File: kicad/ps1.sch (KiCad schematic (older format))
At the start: 35 parts

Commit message: Annotated, regenerated plot
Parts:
- gave numbers to parts that had none: 35
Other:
- moved on the sheet: C1, C10, C11, C12, C13, C14, C2, C3, C4, C5, C6, C7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

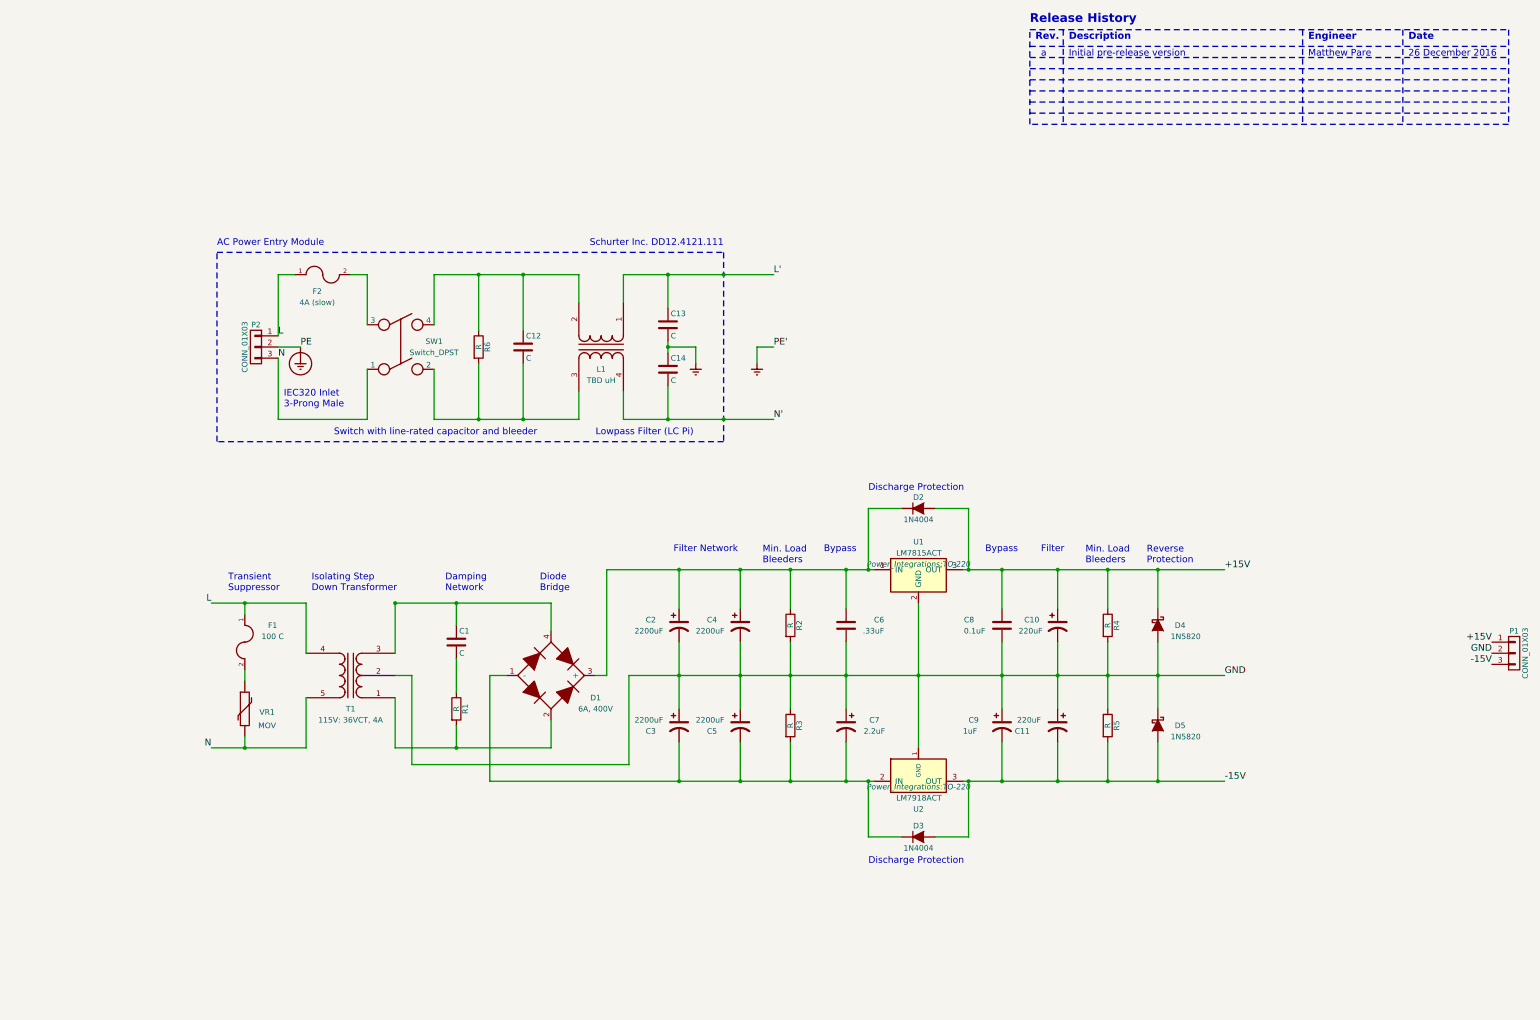
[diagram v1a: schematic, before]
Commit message: Removed power entry block as preparing for pcb layout.
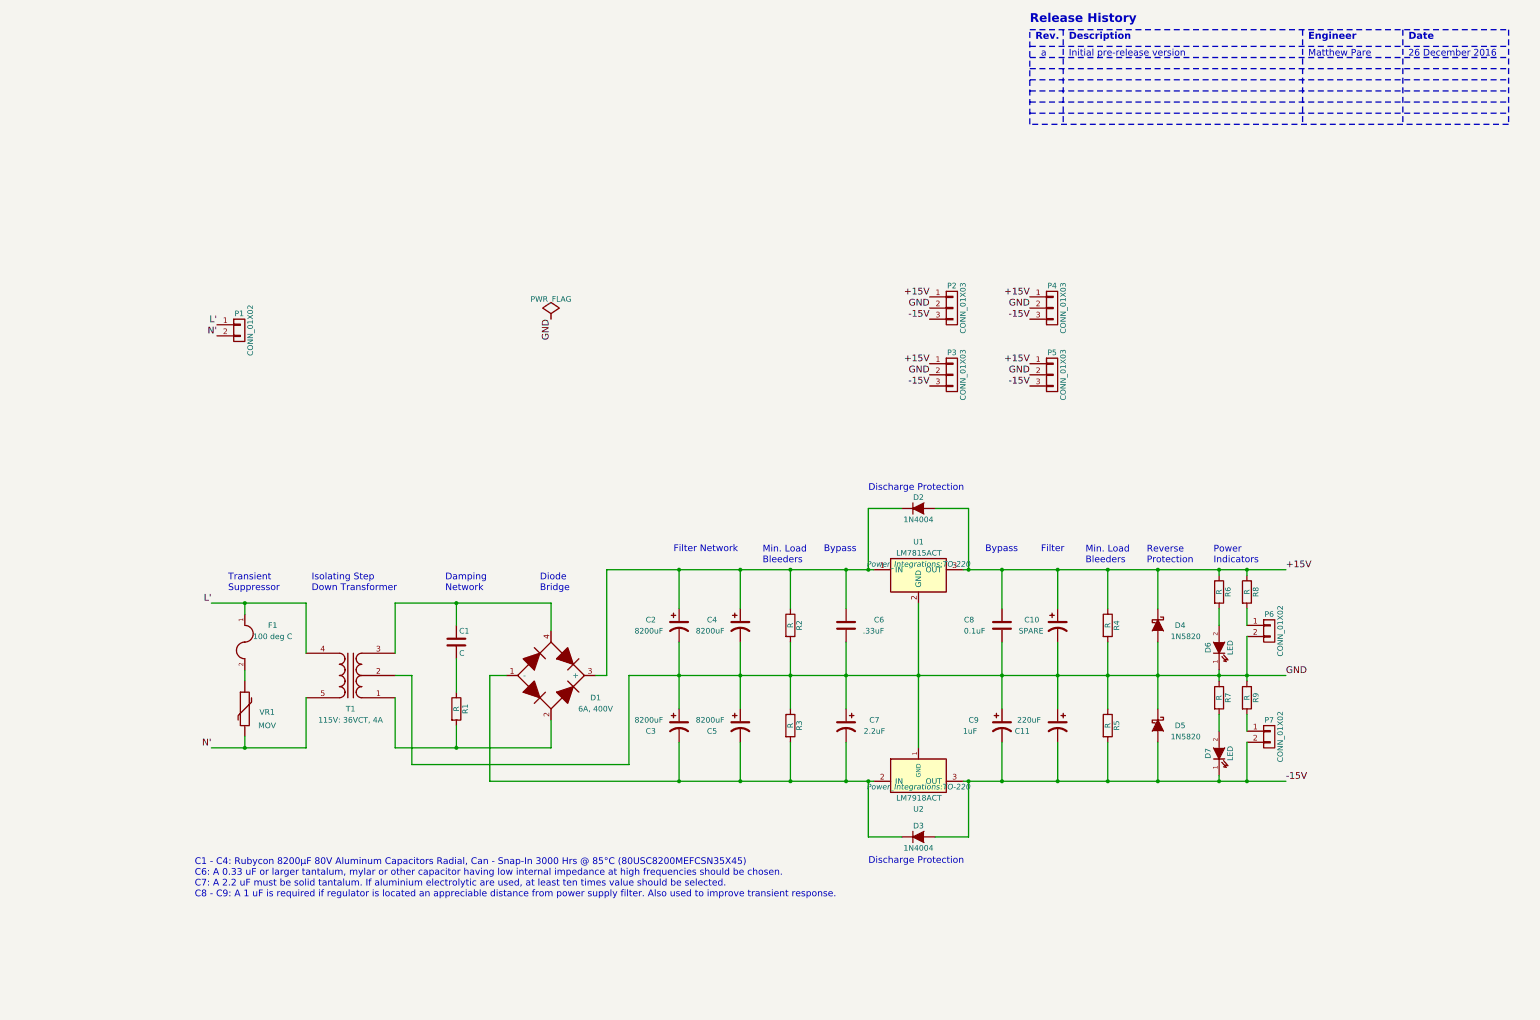
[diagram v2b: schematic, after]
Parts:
- removed C12, C13, C14: C, symbol C
- removed F2: 4A (slow), symbol FUSE
- removed L1: TBD uH, symbol TRANSFO
- removed P1: CONN_01X03, symbol CONN_01X03
- removed SW1: Switch_DPST, symbol Switch_DPST
- added D6, D7: LED, symbol LED
- added P1, P6, P7: CONN_01X02, symbol CONN_01X02
- added P3, P4, P5: CONN_01X03, symbol CONN_01X03
- added R7, R8, R9: R, symbol R
- C10: value 220uF -> SPARE
- C2, C3, C4, C5: value 2200uF -> 8200uF
- F1: value 100 C -> 100 deg C
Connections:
- net Earth_Protective is gone; now on net GND: P2.2 (P2)
- net +15V: now also P2.1 (P1), R6.1, P3.1 (P1), P4.1 (P1), P5.1 (P1), R8.1
- net -15V: now also P2.3 (P3), D7.1 (K), P3.3 (P3), P4.3 (P3), P5.3 (P3), P7.2 (P2)
- net GND: now also D6.1 (K), P3.2 (P2), P4.2 (P2), P5.2 (P2), P6.2 (P2), R7.1, R9.1
- net L': now also F1.1, T1.4 (S1), P1.1 (P1)
- net N': now also T1.5 (S2), VR1.2, P1.2 (P2)
- net at R6.2: now also D6.2 (A)
- removed net L: F1.1, P2.1 (P1), T1.4 (S1)
- removed net N: P2.3 (P3), T1.5 (S2), VR1.2
- new net: P6.1 (P1), R8.2
- new net: D7.2 (A), R7.2
- new net: P7.1 (P1), R9.2
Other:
- note added: "C1 - C4: Rubycon 8200µF 80V Aluminum Capacitors Radial, Can - Snap-In 3000 Hrs @ 85°C (80USC8200MEFCSN35X45)\nC6: A 0.33 uF or larger tantalum, mylar or other capacitor having low internal impedance at high frequencies should be chosen.\nC7: A 2.2 uF must be solid tantalum. If aluminium electrolytic are used, at least ten times value should be selected.\nC8 - C9: A 1 uF is required if regulator i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"
- note added: "Power\nIndicators"
- note removed: "AC Power Entry Module"
- note removed: "IEC320 Inlet\n3-Prong Male"
- note removed: "Lowpass Filter (LC Pi)"
- note removed: "Schurter Inc. DD12.4121.111"
- note removed: "Switch with line-rated capacitor and bleeder"

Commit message: Replaced output connectors and assigned footprint.
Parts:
- removed P2, P3, P4, P5: CONN_01X03, symbol CONN_01X03
- added P4, P5: CONN_02X06, Connectors_Molex:Molex_MiniFit-JR-5556-12A_2x06x4.20mm_Straight, symbol CONN_02X06
- C10, C11: footprint (none) -> Capacitors_ThroughHole:C_Radial_D22_L41_P10
- C2, C3, C4, C5: footprint (none) -> Capacitors_ThroughHole:C_Radial_D35_L51_P10
- D2, D3, D4, D5: footprint (none) -> Diodes_ThroughHole:Diode_DO-41_SOD81_Horizontal_RM10
- D6, D7: footprint (none) -> LEDs:LED_0805
- P2: renamed from P6; footprint (none) -> Pin_Headers:Pin_Header_Angled_1x02
- P3: renamed from P7; footprint (none) -> Pin_Headers:Pin_Header_Angled_1x02
- R2, R3: footprint (none) -> Resistors_ThroughHole:Resistor_Ceramic_Horizontal_L23mm-W9mm-H9mm-p30mm
- R4, R5: footprint (none) -> Resistors_ThroughHole:Resistor_Ceramic_Horizontal_L19mm-W8mm-H8mm-p25mm
- R6, R7, R8, R9: footprint (none) -> Resistors_SMD:R_0805_HandSoldering

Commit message: Removed transient suppressor and added transformer receptacle. Transient suppressor was removed because this board is designed to be all cold side. Use shrink tube wrapped mini board to inline suppressor between power entry module and transformer.
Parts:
- removed F1: 100 deg C, symbol FUSE
- removed P1: CONN_01X02, symbol CONN_01X02
- removed T1: 115V: 36VCT, 4A, symbol TRANSFO4
- removed VR1: MOV, symbol VR
- added P1: CONN_01X03, Molex Mini-Fit Jr. Vertical Single Row Header 39-30-1039, symbol CONN_01X03
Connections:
- net labels added: +18V, -18V
- net labels removed: L', N'
- wire segments 72 -> 59
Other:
- note added: "-"
- note removed: "26 December 2016"
- note removed: "Initial pre-release version"
- note removed: "Isolating Step\nDown Transformer"
- note removed: "Matthew Pare"
- note removed: "Transient\nSuppressor"
- note removed: "a"
- moved on the sheet: C1, C10, C11, C2, C3, C4, C5, C6, C7, C8, C9, D1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

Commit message: Minor updates as picking BOM
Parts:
- D4, D5: value 1N5820 -> 1N5822
- R1: value R -> 20
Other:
- note added: "Mating Receptacle Molex Mini-Fit Single \nRow Receptacle 39-01-4031"
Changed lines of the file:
@@
 P 1850 4600
 F 0 "R1" V 1930 4600 50  0000 C CNN
-F 1 "R" V 1850 4600 50  0000 C CNN
+F 1 "20" V 1850 4600 50  0000 C CNN
 F 2 "" V 1780 4600 50  0001 C CNN
 F 3 "" H 1850 4600 50  0000 C CNN
@@
 P 8150 3850
 F 0 "D4" V 8150 4050 50  0000 C CNN
-F 1 "1N5820" V 8250 4100 50  0000 C CNN
+F 1 "1N5822" V 8250 4100 50  0000 C CNN
 F 2 "Diodes_ThroughHole:Diode_DO-41_SOD81_Horizontal_RM10" H 8150 3850 50  0001 C CNN
 F 3 "" H 8150 3850 50  0000 C CNN
@@
 P 8150 4750
 F 0 "D5" V 8150 4950 50  0000 C CNN
-F 1 "1N5820" V 8250 5000 50  0000 C CNN
+F 1 "1N5822" V 8250 5000 50  0000 C CNN
 F 2 "Diodes_ThroughHole:Diode_DO-41_SOD81_Horizontal_RM10" H 8150 4750 50  0001 C CNN
 F 3 "" H 8150 4750 50  0000 C CNN
@@
 Text Label 1300 4950 2    60   ~ 0
 -18V
+Text Notes 800  1900 0    60   ~ 0
+Mating Receptacle Molex Mini-Fit Single \nRow Receptacle 39-01-4031
 $EndSCHEMATC

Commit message: Various schematic, pcb and footprint modifications. PCB layout left in first schematic order rough fit. Very large layout, need to get creative and find enclosure.
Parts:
- C1: value C -> 0.1uF; footprint (none) -> Resistors_ThroughHole:Resistor_Horizontal_RM10mm
- C2, C3, C4, C5: footprint Capacitors_ThroughHole:C_Radial_D35_L51_P10 -> ps1:C_Radial_D35_L51_P10
- C6, C7, C8: footprint (none) -> Capacitors_ThroughHole:C_Disc_D7.5_P5
- C9: footprint (none) -> Capacitors_ThroughHole:C_Disc_D12_P7.75
- D1: footprint (none) -> ps1:Diode_Bridge_18.5x5.5
- P1: footprint Molex Mini-Fit Jr. Vertical Single Row Header 39-30-1039 -> ps1:Molex_Mini-Fit_JR-5566-03x3x
- P2, P3: footprint Pin_Headers:Pin_Header_Angled_1x02 -> Pin_Headers:Pin_Header_Straight_1x02
- R1: footprint (none) -> Resistors_ThroughHole:Resistor_Horizontal_RM25mm
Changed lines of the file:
@@
 F 0 "C2" H 3550 3900 50  0000 L CNN
 F 1 "8200uF" H 3450 3800 50  0000 L CNN
-F 2 "Capacitors_ThroughHole:C_Radial_D35_L51_P10" H 3850 3850 50  0001 C CNN
+F 2 "ps1:C_Radial_D35_L51_P10" H 3850 3850 50  0001 C CNN
 F 3 "" H 3850 3850 50  0000 C CNN
 	1    3850 3850
@@
 F 0 "C3" H 3550 4700 50  0000 L CNN
 F 1 "8200uF" H 3450 4800 50  0000 L CNN
-F 2 "Capacitors_ThroughHole:C_Radial_D35_L51_P10" H 3850 4750 50  0001 C CNN
+F 2 "ps1:C_Radial_D35_L51_P10" H 3850 4750 50  0001 C CNN
 F 3 "" H 3850 4750 50  0000 C CNN
 	1    3850 4750
@@
 F 0 "C8" H 7000 3900 50  0000 L CNN
 F 1 "0.1uF" H 6900 3800 50  0000 L CNN
-F 2 "" H 6788 3700 50  0001 C CNN
+F 2 "Capacitors_ThroughHole:C_Disc_D7.5_P5" H 6788 3700 50  0001 C CNN
 F 3 "" H 6750 3850 50  0000 C CNN
 	1    6750 3850
@@
 P 1850 4000
 F 0 "C1" H 1875 4100 50  0000 L CNN
-F 1 "C" H 1875 3900 50  0000 L CNN
-F 2 "" H 1888 3850 50  0001 C CNN
+F 1 "0.1uF" H 1875 3900 50  0000 L CNN
+F 2 "Resistors_ThroughHole:Resistor_Horizontal_RM10mm" H 1888 3850 50  0001 C CNN
 F 3 "" H 1850 4000 50  0000 C CNN
 	1    1850 4000
@@
 F 0 "R1" V 1930 4600 50  0000 C CNN
 F 1 "20" V 1850 4600 50  0000 C CNN
-F 2 "" V 1780 4600 50  0001 C CNN
+F 2 "Resistors_ThroughHole:Resistor_Horizontal_RM25mm" V 1780 4600 50  0001 C CNN
 F 3 "" H 1850 4600 50  0000 C CNN
 	1    1850 4600
@@
 F 0 "D1" H 3100 4100 50  0000 C CNN
 F 1 "6A, 400V" H 3100 4000 50  0000 C CNN
-F 2 "" H 2700 4300 50  0001 C CNN
+F 2 "ps1:Diode_Bridge_18.5x5.5" H 2700 4300 50  0001 C CNN
 F 3 "" H 2700 4300 50  0000 C CNN
 	1    2700 4300
@@
 F 0 "C4" H 4100 3900 50  0000 L CNN
 F 1 "8200uF" H 4000 3800 50  0000 L CNN
-F 2 "Capacitors_ThroughHole:C_Radial_D35_L51_P10" H 4400 3850 50  0001 C CNN
+F 2 "ps1:C_Radial_D35_L51_P10" H 4400 3850 50  0001 C CNN
 F 3 "" H 4400 3850 50  0000 C CNN
 	1    4400 3850
@@
 F 0 "C5" H 4100 4700 50  0000 L CNN
 F 1 "8200uF" H 4000 4800 50  0000 L CNN
-F 2 "Capacitors_ThroughHole:C_Radial_D35_L51_P10" H 4400 4750 50  0001 C CNN
+F 2 "ps1:C_Radial_D35_L51_P10" H 4400 4750 50  0001 C CNN
 F 3 "" H 4400 4750 50  0000 C CNN
 	1    4400 4750
@@
 F 0 "C6" H 5600 3900 50  0000 L CNN
 F 1 ".33uF" H 5500 3800 50  0000 L CNN
-F 2 "" H 5388 3700 50  0001 C CNN
+F 2 "Capacitors_ThroughHole:C_Disc_D7.5_P5" H 5388 3700 50  0001 C CNN
 F 3 "" H 5350 3850 50  0000 C CNN
 	1    5350 3850
@@
 F 0 "C9" H 6450 4800 50  0000 L CNN
 F 1 "1uF" H 6400 4700 50  0000 L CNN
-F 2 "" H 6750 4750 50  0001 C CNN
+F 2 "Capacitors_ThroughHole:C_Disc_D12_P7.75" H 6750 4750 50  0001 C CNN
 F 3 "" H 6750 4750 50  0000 C CNN
 	1    6750 4750
@@
 F 0 "C7" H 5050 4800 50  0000 L CNN
 F 1 "2.2uF" H 5000 4700 50  0000 L CNN
-F 2 "" H 5350 4750 50  0001 C CNN
+F 2 "Capacitors_ThroughHole:C_Disc_D7.5_P5" H 5350 4750 50  0001 C CNN
 F 3 "" H 5350 4750 50  0000 C CNN
 	1    5350 4750
@@
 F 0 "P2" H 9150 4050 50  0000 C CNN
 F 1 "CONN_01X02" V 9250 3900 50  0000 C CNN
-F 2 "Pin_Headers:Pin_Header_Angled_1x02" H 9150 3900 50  0001 C CNN
+F 2 "Pin_Headers:Pin_Header_Straight_1x02" H 9150 3900 50  0001 C CNN
 F 3 "" H 9150 3900 50  0000 C CNN
 	1    9150 3900
@@
 F 0 "P3" H 9150 5000 50  0000 C CNN
 F 1 "CONN_01X02" V 9250 4850 50  0000 C CNN
-F 2 "Pin_Headers:Pin_Header_Angled_1x02" H 9150 4850 50  0001 C CNN
+F 2 "Pin_Headers:Pin_Header_Straight_1x02" H 9150 4850 50  0001 C CNN
 F 3 "" H 9150 4850 50  0000 C CNN
 	1    9150 4850
@@
 F 0 "P1" H 1750 1350 50  0000 C CNN
 F 1 "CONN_01X03" V 1850 1150 50  0000 C CNN
-F 2 "Molex Mini-Fit Jr. Vertical Single Row Header 39-30-1039" H 1750 750 50  0000 C CNN
+F 2 "ps1:Molex_Mini-Fit_JR-5566-03x3x" H 1750 750 50  0001 C CNN
 F 3 "" H 1750 1150 50  0000 C CNN
 	1    1750 1150

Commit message: Umm, it has been a while since I committed to something.
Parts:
- D6, D7: symbol LED -> LED-RESCUE-ps1
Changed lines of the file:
@@
 EESchema Schematic File Version 2
+LIBS:ps1-rescue
 LIBS:power
 LIBS:device
@@
 C1 - C4: Rubycon 8200µF 80V Aluminum Capacitors Radial, Can - Snap-In 3000 Hrs @ 85°C (80USC8200MEFCSN35X45)\nC6: A 0.33 uF or larger tantalum, mylar or other capacitor having low internal impedance at high frequencies should be chosen.\nC7: A 2.2 uF must be solid tantalum. If aluminium electrolytic are used, at least ten times value should be selected.\nC8 - C9: A 1 uF is required if regulator is located an appreciable distance from power supply filter. Also used to improve transient response.\n
 $Comp
-L LED D6
+L LED-RESCUE-ps1 D6
 U 1 1 5869BAB4
 P 8700 4050
@@
 $EndComp
 $Comp
-L LED D7
+L LED-RESCUE-ps1 D7
 U 1 1 5869C04C
 P 8700 5000
@@
 Text Notes 800  1900 0    60   ~ 0
 Mating Receptacle Molex Mini-Fit Single \nRow Receptacle 39-01-4031
+Entry Wire Line
+	11600 4800 11700 4900
 $EndSCHEMATC
